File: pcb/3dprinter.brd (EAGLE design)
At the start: 69.5 x 56 mm, 119 parts, among them IC1 NRF51822, IC1_REG REGULATOR, IC2_REG LP2985-3V3, Q1_BED MOSFET, Q1_FAN1 MOSFETSOT23, Q1_FAN2 MOSFETSOT23, Q1_NOZ MOSFET, Y1 CRYSTAL

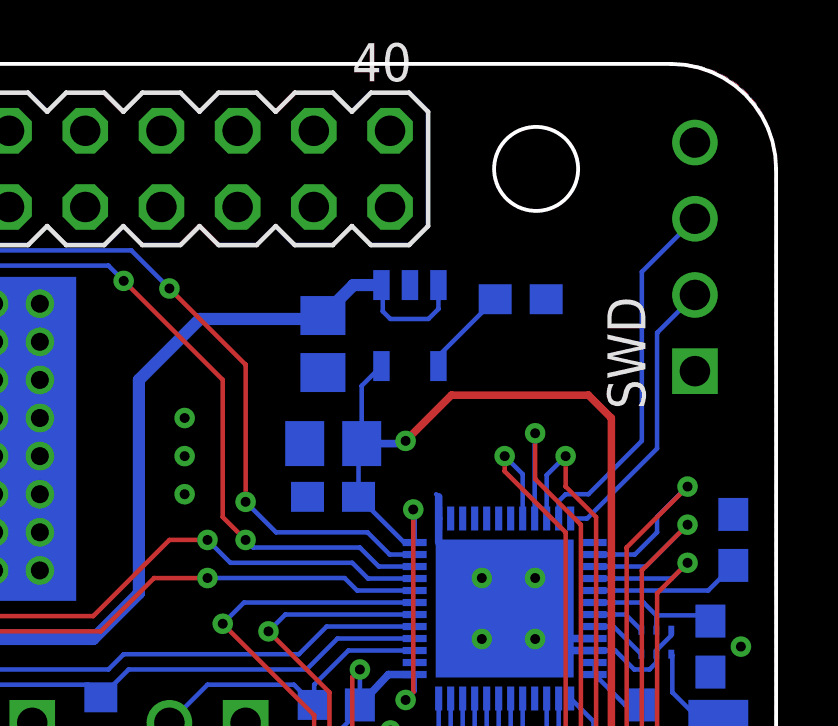
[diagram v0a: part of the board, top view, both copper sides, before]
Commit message: Added button and led
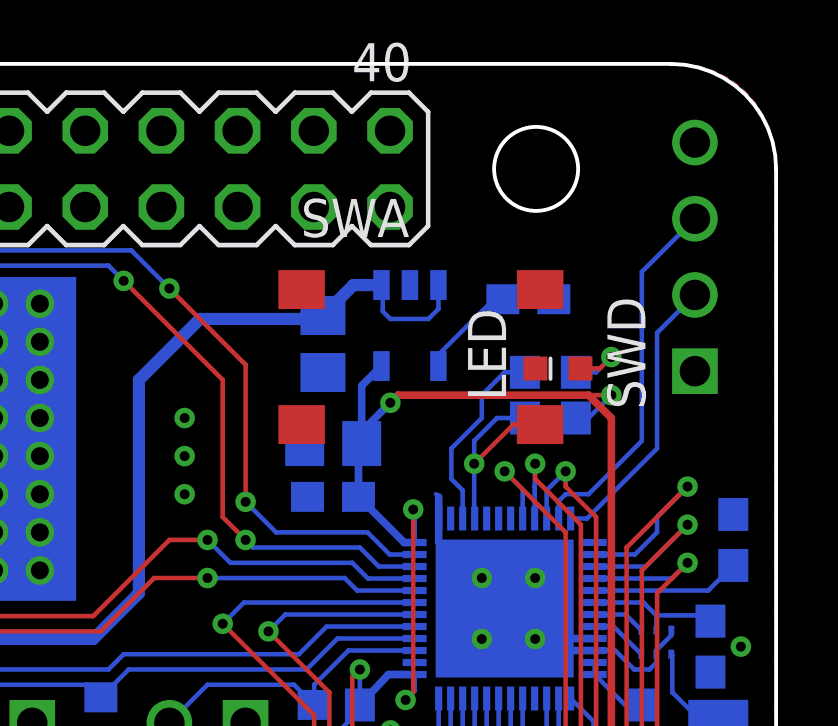
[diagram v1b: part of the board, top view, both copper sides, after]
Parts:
- added LED: RGBLED, 3dprinter:RGBLED
- added R1_LED: 100R, 3dprinter:R0603
- added R1_SWA: 10k, 3dprinter:R0603
- added SWA: BUTTON, 3dprinter:BUTTON
- moved C4_REG 0.25 mm to (61.2, 48.2)
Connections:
- removed net P0.09: IC1.15
- removed net P0.10: IC1.16
- new net LED: IC1.15, R1_LED.1
- new net LEDA: LED.A, R1_LED.2
- new net SWA: IC1.16, R1_SWA.1, SWA.4
- net +3V3: now also R1_SWA.2
- net GND: now also LED.C, SWA.1, SWA.2
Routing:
- net SWA: track 0.00 -> 7.34 mm, vias 0 -> 1
- net LED: track 0.00 -> 6.44 mm
- net LEDA: track 0.00 -> 2.58 mm, vias 0 -> 1
- net +3V3: track 176.4 -> 178.9 mm, vias 15 -> 16
- net DIR_M2: track 46.9 -> 44.8 mm
- net EN_M2: track 52.1 -> 51.0 mm
- net STEP_M2: track 46.8 -> 46.0 mm

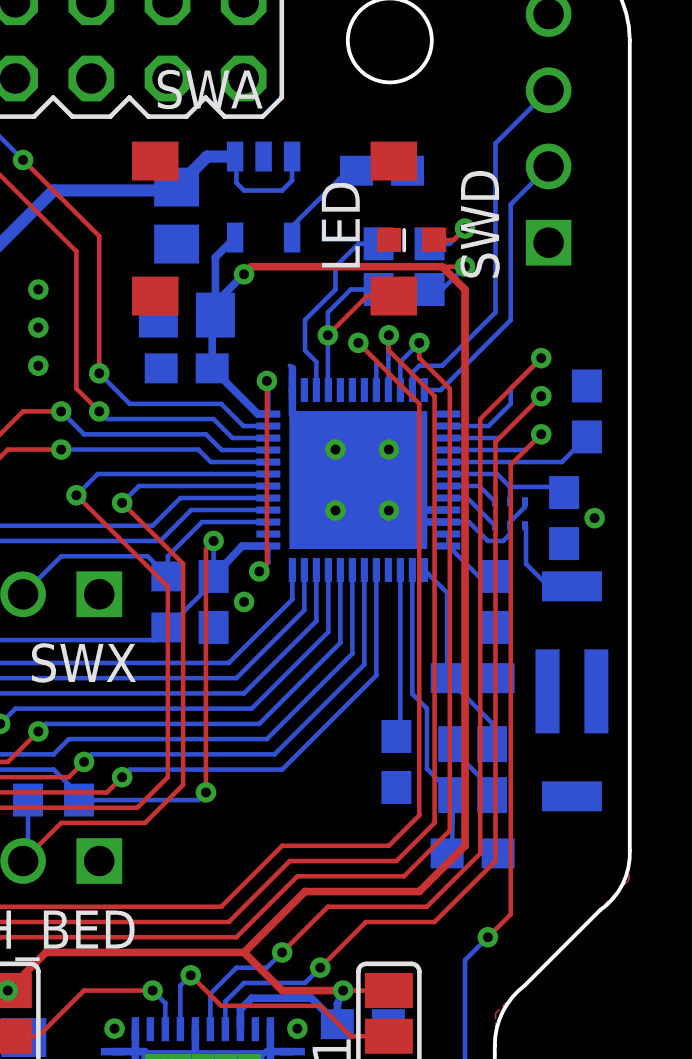
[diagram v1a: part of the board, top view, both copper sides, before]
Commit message: Added testpads ERC/DRC OK
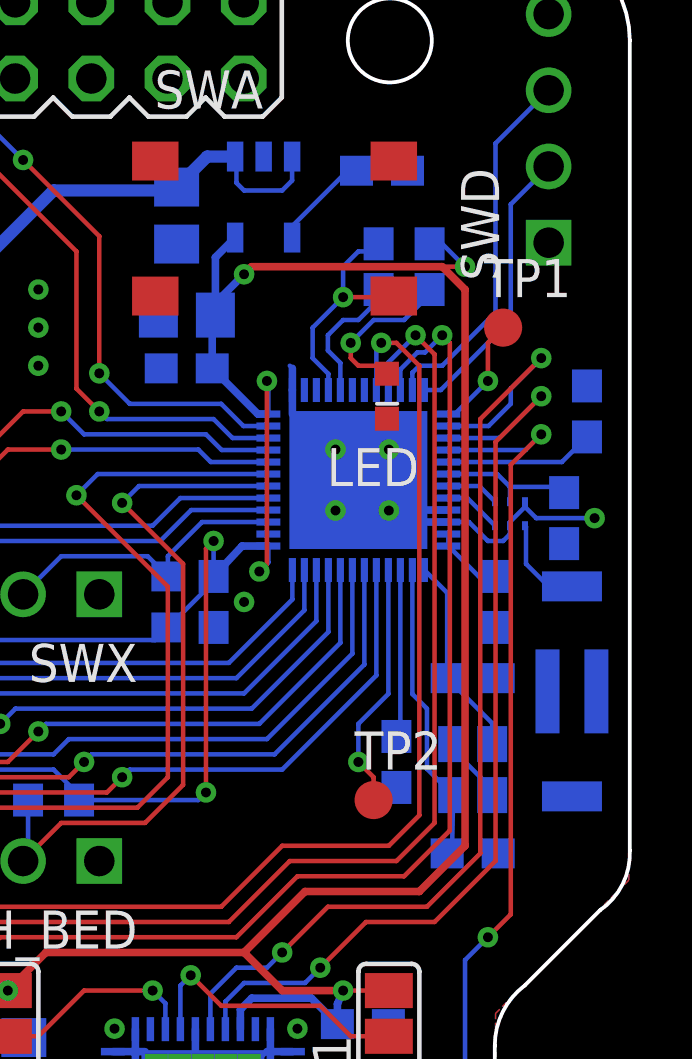
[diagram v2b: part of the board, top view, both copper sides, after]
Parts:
- added TP1, TP2: TPB1,27, 3dprinter:B1,27
- moved LED 5.27 mm to (61.4, 40.6), turned to 0 degrees
- moved R1_LED 1.52 mm to (62.0, 44.2)
- moved R1_SWA 1.52 mm to (62.0, 45.7)
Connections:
- removed net P0.11: IC1.17
- new net P0.09: IC1.15
- net LED: now also IC1.17; no longer IC1.15
- net P0.17: now also TP1.TP
- net P0.21: now also TP2.TP
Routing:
- net P0.21: track 0.00 -> 8.29 mm, vias 0 -> 1
- net P0.17: track 0.00 -> 3.76 mm, vias 0 -> 1
- net LEDA: track 2.58 -> 5.39 mm
- net GND: track 73.7 -> 76.2 mm
- net LED: track 6.44 -> 4.52 mm
- net EN_M2: track 51.0 -> 51.7 mm
- net SWA: track 7.34 -> 7.95 mm

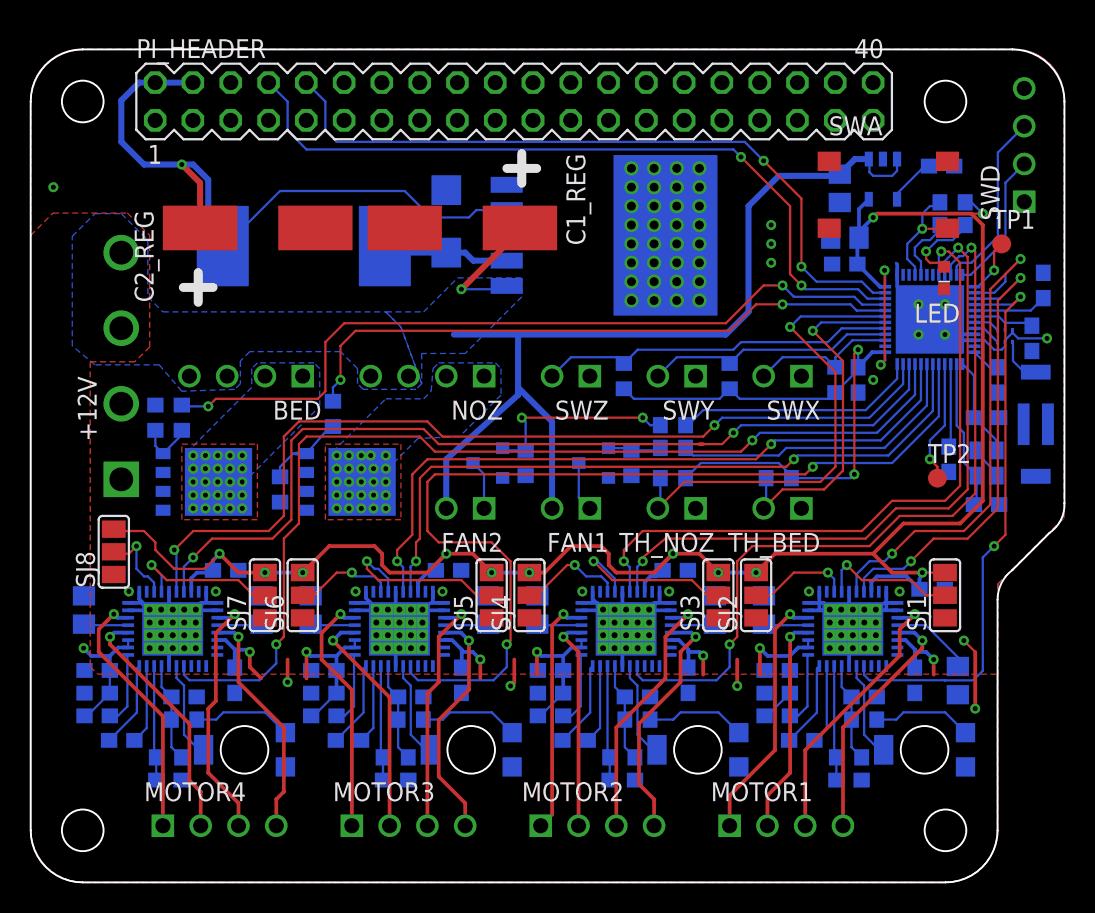
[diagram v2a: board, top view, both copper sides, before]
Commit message: Top/Bot silkscreen and clearance
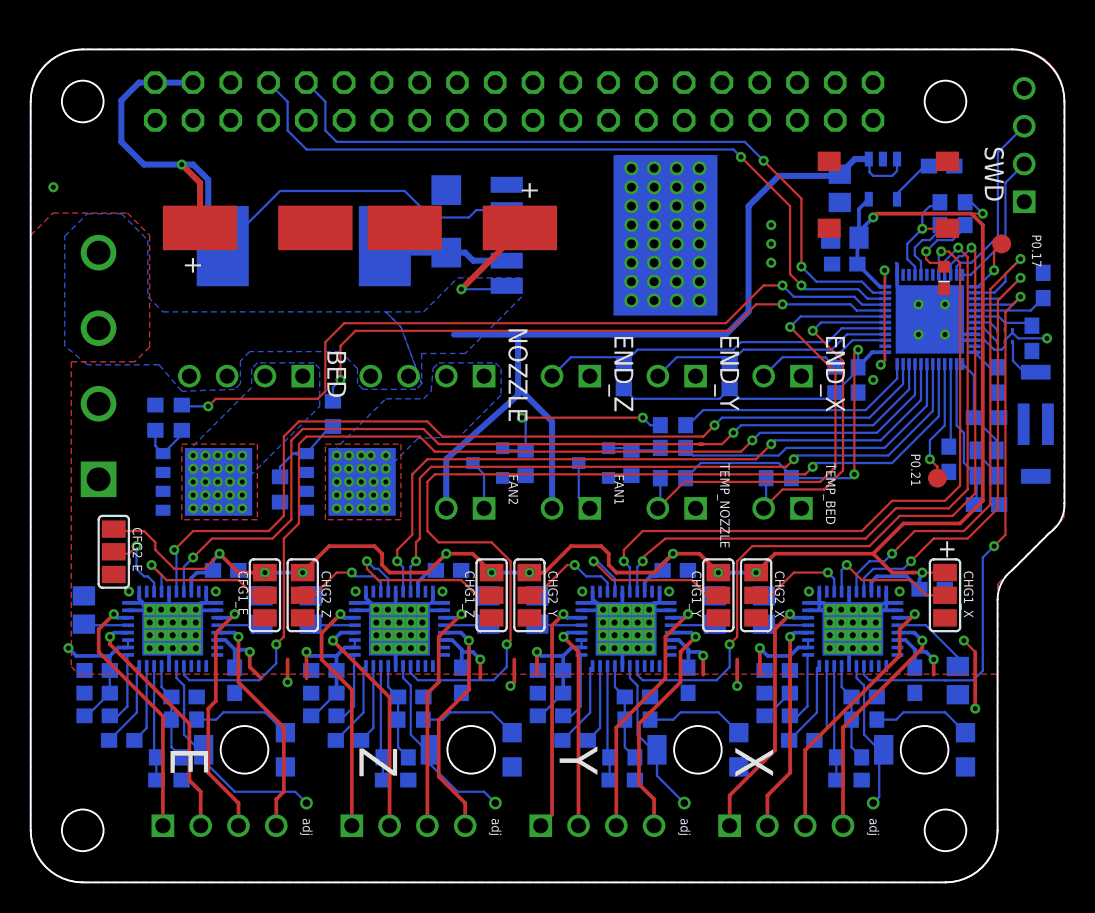
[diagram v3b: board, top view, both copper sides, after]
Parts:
- moved +12V 1.52 mm to (4.56, 34.7)
- renumbered MOTOR1 to X, MOTOR2 to Y, MOTOR3 to Z, MOTOR4 to E, NOZ to NOZZLE, SJ1 to CHG1_X, SJ2 to CHG2_X, SJ3 to CHG1_Y, SJ4 to CHG2_Y, SJ5 to CHG1_Z, SJ6 to CHG2_Z, SJ7 to CFG1_E, SJ8 to CFG2_E, SWX to END_X, SWY to END_Y, SWZ to END_Z, TH_BED to TEMP_BED, TH_NOZ to TEMP_NOZZLE, TP1 to P0.17, TP2 to P0.21
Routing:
- net AIN_M4: track 6.56 -> 15.4 mm, vias 0 -> 1
- net AIN_M3: track 6.56 -> 13.0 mm, vias 0 -> 1
- net AIN_M2: track 6.56 -> 10.9 mm, vias 0 -> 1
- net AIN_M1: track 6.56 -> 10.3 mm, vias 0 -> 1
- net +12V: track 134.5 -> 135.5 mm
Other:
- board text added: "+"
- board text added: "adj"

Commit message: Silk screen
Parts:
- moved P0.21 5.14 mm to (56.6, 30.0)
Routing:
- net P0.21: track 8.29 -> 12.7 mm
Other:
- board text added: "3D Printer board PCB rev1 #"
